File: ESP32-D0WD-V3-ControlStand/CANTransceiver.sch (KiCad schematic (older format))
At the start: 14 parts

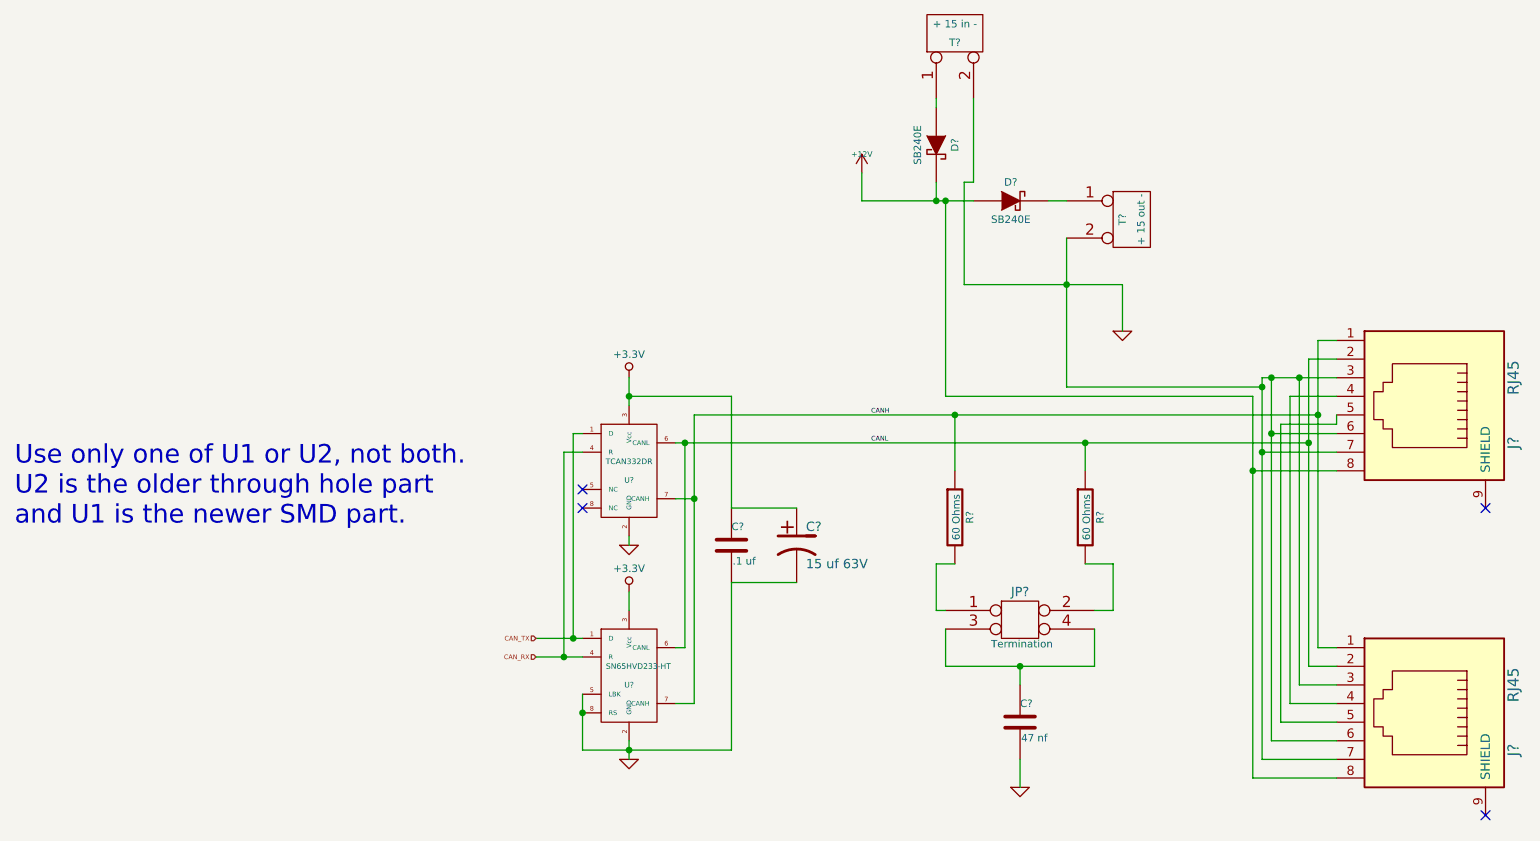
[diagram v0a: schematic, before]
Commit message: Completed parts spec for ESP32-D0WD-V3-ControlStand.
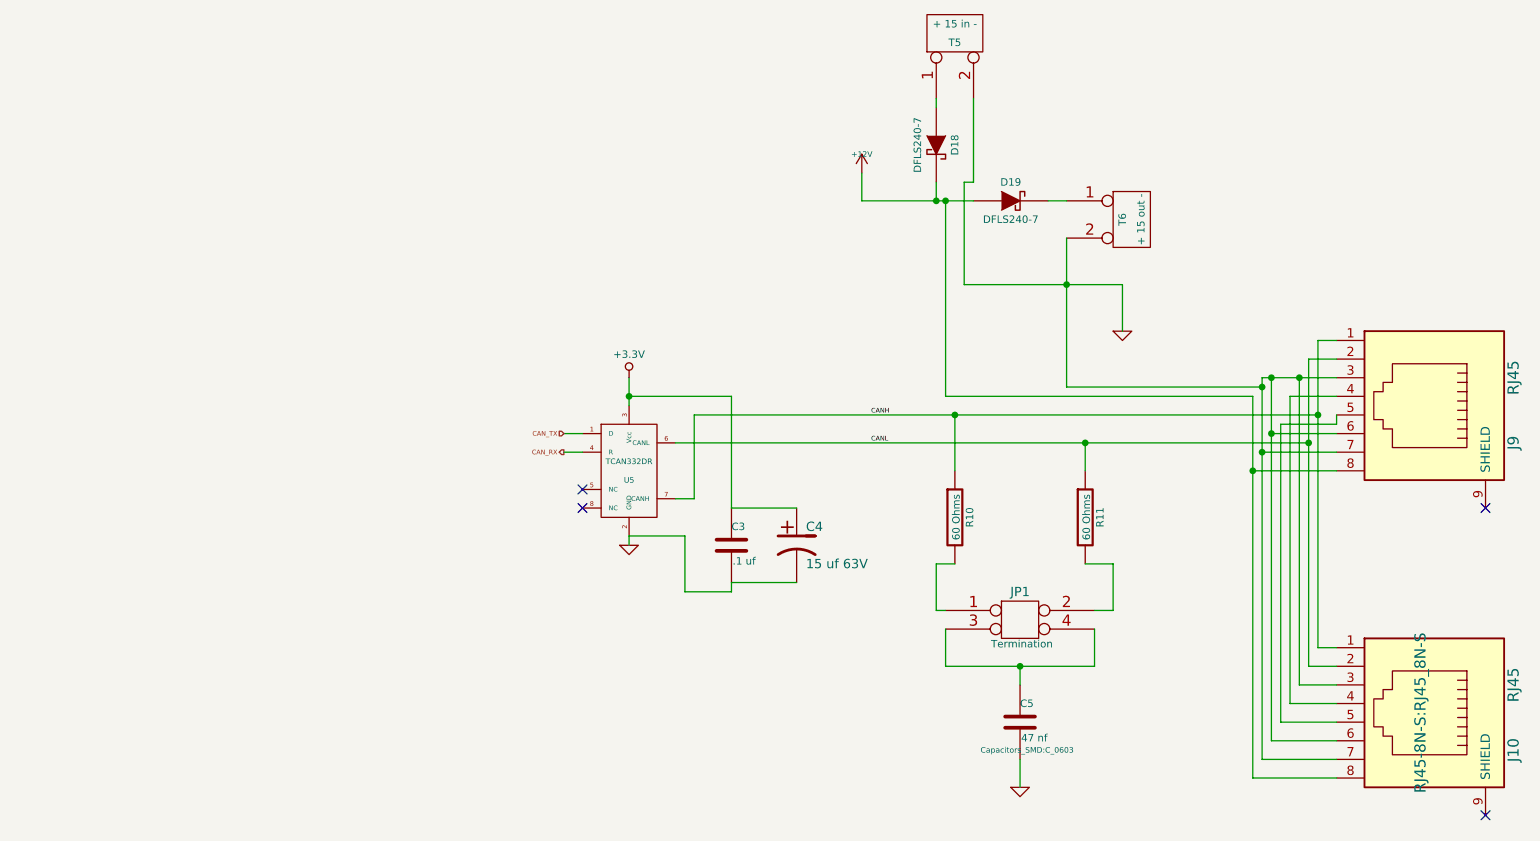
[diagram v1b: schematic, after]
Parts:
- removed U?: SN65HVD233-HT, ~, symbol SN65HVD233-HT
- C3: renamed from C?; footprint ~ -> Capacitors_SMD:C_0603; Mouser Part Number 21RZ310-RC -> 710-885012206095
- C4: renamed from C?; footprint ~ -> Capacitors_SMD:CP_Elec_4x5.7; Mouser Part Number 710-860080773002 -> 647-UUD1C150MCL
- C5: renamed from C?; footprint ~ -> Capacitors_SMD:C_0603; Mouser Part Number 75-1C10Z5U473M050B -> 710-885012206093
- D18, D19: renamed from D?; value SB240E -> DFLS240-7; footprint ~ -> Diodes_SMD:D_PowerDI-123; Mouser Part Number 625-SB240-E3 -> 621-DFLS240-7
- J10, J9: renamed from J?; footprint (none) -> RJ45-8N-S:RJ45_8N-S
- JP1: renamed from JP?; footprint (none) -> Pin_Headers:Pin_Header_Straight_2x02_Pitch2.54mm
- R10, R11: renamed from R?; footprint ~ -> Resistors_SMD:R_1206; Mouser Part Number 71-RN60C60R0B/R -> 71-CRCW120660R0KNAIF
- T5, T6: renamed from T?; footprint (none) -> Terminal_Blocks:TerminalBlock_Pheonix_MPT-2.54mm_2pol
- U5: renamed from U?; footprint ~ -> Housings_SOIC:SOIC-8_3.9x4.9mm_Pitch1.27mm
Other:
- note removed: "Use only one of U1 or U2, not both.\nU2 is the older through hole part\nand U1 is the newer SMD part."

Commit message: Working on the PCB Layout.
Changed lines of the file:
@@
 LIBS:mcp73871
 LIBS:lm2574n-5
+LIBS:mechanical
+LIBS:graphic_symbols
 LIBS:ESP32-D0WD-V3-ControlStand-cache
 EELAYER 25 0
@@
 $EndComp
 $Comp
-L +3.3V-RESCUE-ESP32ControlStand #PWR40
+L +3.3V-RESCUE-ESP32ControlStand #PWR040
 U 1 1 62DF1263
 P 4100 2900
-F 0 "#PWR40" H 4100 3000 40  0001 C CNN
+F 0 "#PWR040" H 4100 3000 40  0001 C CNN
 F 1 "+3.3V" H 4100 3025 40  0000 C CNN
 F 2 "" H 4100 2900 60  0000 C CNN
@@
 $EndComp
 $Comp
-L GND-RESCUE-ESP32ControlStand #PWR41
+L GND-RESCUE-ESP32ControlStand #PWR041
 U 1 1 62DF1265
 P 4100 3800
-F 0 "#PWR41" H 4100 3800 30  0001 C CNN
+F 0 "#PWR041" H 4100 3800 30  0001 C CNN
 F 1 "GND" H 4100 3730 30  0001 C CNN
 F 2 "" H 4100 3800 60  0000 C CNN
@@
 F 0 "C5" H 6200 4850 40  0000 L CNN
 F 1 "47 nf" H 6206 4665 40  0000 L CNN
-F 2 "Capacitors_SMD:C_0603" H 6238 4600 30  0000 C CNN
+F 2 "Capacitors_SMD:C_0603" H 6238 4600 30  0001 C CNN
 F 3 "~" H 6200 4750 60  0000 C CNN
 F 4 "710-885012206093" H 6200 4750 60  0001 C CNN "Mouser Part Number"
@@
 $EndComp
 $Comp
-L GND-RESCUE-ESP32ControlStand #PWR43
+L GND-RESCUE-ESP32ControlStand #PWR042
 U 1 1 62DF126D
 P 6200 5100
-F 0 "#PWR43" H 6200 5100 30  0001 C CNN
+F 0 "#PWR042" H 6200 5100 30  0001 C CNN
 F 1 "GND" H 6200 5030 30  0001 C CNN
 F 2 "" H 6200 5100 60  0000 C CNN
@@
 	7450 3000 7450 5050
 $Comp
-L GND-RESCUE-ESP32ControlStand #PWR44
+L GND-RESCUE-ESP32ControlStand #PWR043
 U 1 1 62DF1272
 P 6750 2650
-F 0 "#PWR44" H 6750 2650 30  0001 C CNN
+F 0 "#PWR043" H 6750 2650 30  0001 C CNN
 F 1 "GND" H 6750 2580 30  0001 C CNN
 F 2 "" H 6750 2650 60  0000 C CNN
@@
 Connection ~ 5800 1950
 $Comp
-L +12V #PWR42
+L +12V #PWR044
 U 1 1 62DF1275
 P 5350 1800
-F 0 "#PWR42" H 5350 1750 20  0001 C CNN
+F 0 "#PWR044" H 5350 1750 20  0001 C CNN
 F 1 "+12V" H 5350 1900 30  0000 C CNN
 F 2 "" H 5350 1800 60  0000 C CNN

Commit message: Completed V0.0 PCB.
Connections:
- net +3.3V renamed +3V3
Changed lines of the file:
@@
 $EndComp
 $Comp
-L +3.3V-RESCUE-ESP32ControlStand #PWR040
+L +3.3V #PWR042
 U 1 1 62DF1263
 P 4100 2900
-F 0 "#PWR040" H 4100 3000 40  0001 C CNN
+F 0 "#PWR042" H 4100 3000 40  0001 C CNN
 F 1 "+3.3V" H 4100 3025 40  0000 C CNN
 F 2 "" H 4100 2900 60  0000 C CNN
@@
 $EndComp
 $Comp
-L GND-RESCUE-ESP32ControlStand #PWR041
+L GND #PWR043
 U 1 1 62DF1265
 P 4100 3800
-F 0 "#PWR041" H 4100 3800 30  0001 C CNN
+F 0 "#PWR043" H 4100 3800 30  0001 C CNN
 F 1 "GND" H 4100 3730 30  0001 C CNN
 F 2 "" H 4100 3800 60  0000 C CNN
@@
 $EndComp
 $Comp
-L GND-RESCUE-ESP32ControlStand #PWR042
+L GND #PWR044
 U 1 1 62DF126D
 P 6200 5100
-F 0 "#PWR042" H 6200 5100 30  0001 C CNN
+F 0 "#PWR044" H 6200 5100 30  0001 C CNN
 F 1 "GND" H 6200 5030 30  0001 C CNN
 F 2 "" H 6200 5100 60  0000 C CNN
@@
 	7450 3000 7450 5050
 $Comp
-L GND-RESCUE-ESP32ControlStand #PWR043
+L GND #PWR045
 U 1 1 62DF1272
 P 6750 2650
-F 0 "#PWR043" H 6750 2650 30  0001 C CNN
+F 0 "#PWR045" H 6750 2650 30  0001 C CNN
 F 1 "GND" H 6750 2580 30  0001 C CNN
 F 2 "" H 6750 2650 60  0000 C CNN
@@
 Connection ~ 5800 1950
 $Comp
-L +12V #PWR044
+L +12V #PWR046
 U 1 1 62DF1275
 P 5350 1800
-F 0 "#PWR044" H 5350 1750 20  0001 C CNN
+F 0 "#PWR046" H 5350 1750 20  0001 C CNN
 F 1 "+12V" H 5350 1900 30  0000 C CNN
 F 2 "" H 5350 1800 60  0000 C CNN

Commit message: About halfway done.
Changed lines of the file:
@@
 $EndComp
 $Comp
-L +3.3V #PWR042
+L +3.3V #PWR040
 U 1 1 62DF1263
 P 4100 2900
-F 0 "#PWR042" H 4100 3000 40  0001 C CNN
+F 0 "#PWR040" H 4100 3000 40  0001 C CNN
 F 1 "+3.3V" H 4100 3025 40  0000 C CNN
 F 2 "" H 4100 2900 60  0000 C CNN
@@
 $EndComp
 $Comp
-L GND #PWR043
+L GND #PWR041
 U 1 1 62DF1265
 P 4100 3800
-F 0 "#PWR043" H 4100 3800 30  0001 C CNN
+F 0 "#PWR041" H 4100 3800 30  0001 C CNN
 F 1 "GND" H 4100 3730 30  0001 C CNN
 F 2 "" H 4100 3800 60  0000 C CNN
@@
 $EndComp
 $Comp
-L GND #PWR044
+L GND #PWR042
 U 1 1 62DF126D
 P 6200 5100
-F 0 "#PWR044" H 6200 5100 30  0001 C CNN
+F 0 "#PWR042" H 6200 5100 30  0001 C CNN
 F 1 "GND" H 6200 5030 30  0001 C CNN
 F 2 "" H 6200 5100 60  0000 C CNN
@@
 F 0 "J10" H 8550 5200 60  0000 C CNN
 F 1 "RJ45" H 8200 5200 60  0000 C CNN
-F 2 "RJ45-8N-S:RJ45_8N-S" H 8350 4700 60  0000 C CNN
+F 2 "RJ45-8N-S:RJ45_8N-S" H 8350 4700 60  0001 C CNN
 F 3 "" H 8350 4700 60  0000 C CNN
 F 4 "710-615008144221" H 8350 4700 60  0001 C CNN "Mouser Part Number"
@@
 	7450 3000 7450 5050
 $Comp
-L GND #PWR045
+L GND #PWR043
 U 1 1 62DF1272
 P 6750 2650
-F 0 "#PWR045" H 6750 2650 30  0001 C CNN
+F 0 "#PWR043" H 6750 2650 30  0001 C CNN
 F 1 "GND" H 6750 2580 30  0001 C CNN
 F 2 "" H 6750 2650 60  0000 C CNN
@@
 Connection ~ 5800 1950
 $Comp
-L +12V #PWR046
+L +12V #PWR044
 U 1 1 62DF1275
 P 5350 1800
-F 0 "#PWR046" H 5350 1750 20  0001 C CNN
+F 0 "#PWR044" H 5350 1750 20  0001 C CNN
 F 1 "+12V" H 5350 1900 30  0000 C CNN
 F 2 "" H 5350 1800 60  0000 C CNN
